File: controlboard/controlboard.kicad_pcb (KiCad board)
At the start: 4 copper layers, 65 x 56.5 mm, 167 parts, among them J1 Conn_02x04_Counter_Clockwise, J11 Pololu Voltage Regulator, J2 Conn_02x04_Row_Letter_Last, J27 GPIO, J3 Conn_02x04_Counter_Clockwise, J4 USB_C_Receptacle_USB2.0_14P, J5 Conn_02x04_Row_Letter_First, J6 Conn_02x04_Counter_Clockwise, J7 Screw_Terminal_01x02, J9 mini560 voltage regulator, Q1 PMOS AO3401A, Q2 PMOS AO3401A, SW2 SW_Push TODO FP CHECK, U2 TPS25963x, U3 AMS1117-3.3, U4 CH224K, U5 TPS25963x, U6 TPS25963x

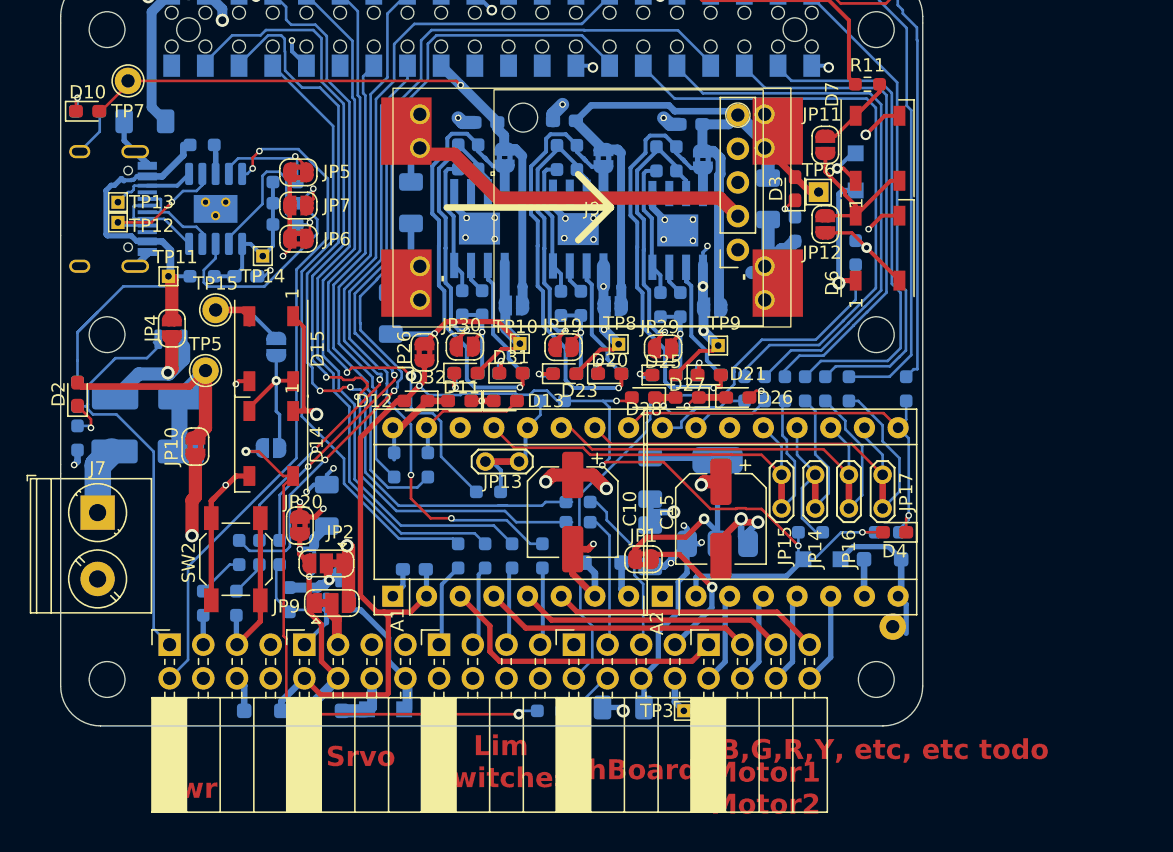
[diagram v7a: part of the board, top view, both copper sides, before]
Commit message: controlboard: fix critical mosfet errors
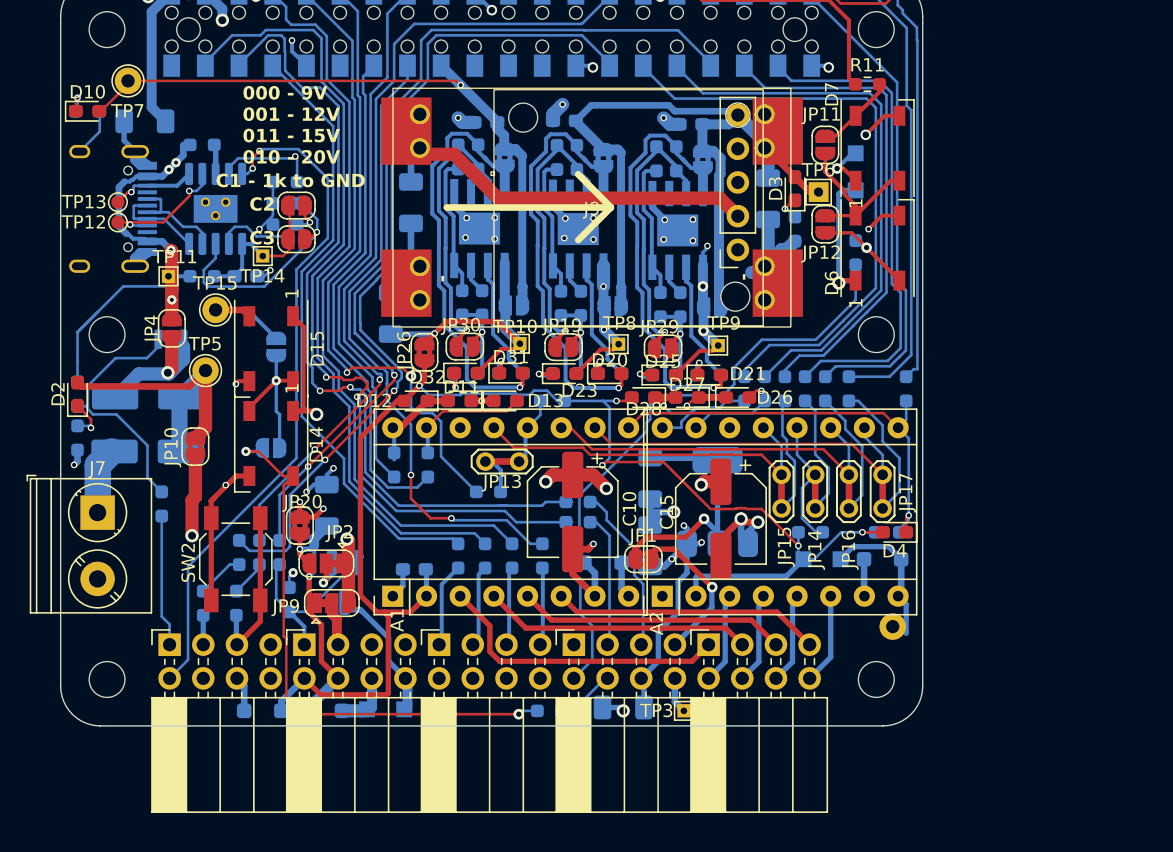
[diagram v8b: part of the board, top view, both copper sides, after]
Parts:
- removed JP5: SolderJumper_2_Bridged, Jumper:SolderJumper-2_P1.3mm_Bridged2Bar_RoundedPad1.0x1.5mm
- added R22: 10k, Resistor_SMD:R_0603_1608Metric_Pad0.98x0.95mm_HandSolder, B.Cu at (107.6, 83.3)
- JP6: value SolderJumper_2_Bridged -> CFG3; footprint Jumper:SolderJumper-2_P1.3mm_Bridged2Bar_RoundedPad1.0x1.5mm -> Jumper:SolderJumper-2_P1.3mm_Open_RoundedPad1.0x1.5mm
- JP7: value SolderJumper_2_Open -> CFG3
- Q1: value PMOS AO3401A -> NMOS AO3400A; footprint Package_TO_SOT_SMD:SOT-23 -> Package_TO_SOT_SMD:SOT-23_Handsoldering
- TP12, TP13: footprint TestPoint:TestPoint_THTPad_1.0x1.0mm_Drill0.5mm -> TestPoint:TestPoint_Pad_D1.0mm
- moved JP7 2.54 mm to (117.8, 63.3)
- moved JP6 2.50 mm to (117.8, 60.8)
- moved Q1 0.69 mm to (121.4, 89.2), turned to -90 degrees
- turned R20 to -90 degrees
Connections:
- net Net-(JP4-A) renamed /Power/VBUS
- J6 pad 7: unconnected-(J6-Pin_7-Pad7) -> GND
- JP6 pad 1: GND -> /Power/CH_VDD
- JP7 pad 1: GND -> /Power/CH_VDD
- Q1 pad 1: Net-(D1-K) -> Net-(JP9-C)
- Q1 pad 3: Net-(JP9-C) -> Net-(D1-K)
- Q2 pad 2: /Power/PWR_SW_B -> Net-(Q2-G)
- R20 pad 1: /MAG_PWM -> GND
- R20 pad 2: Net-(JP9-C) -> /MAG_PWM
- R3 pad 2: /Power/PWR_SW_B -> Net-(Q2-G)
- R4 pad 1: /Power/CH_VDD -> GND
- R5 pad 1: /Power/CH_VDD -> GND
- R6 pad 1: /Power/CH_VDD -> GND
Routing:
- net /CNC/VMOT: track 99.9 -> 158.8 mm
- net /Power/VBUS: track 44.6 -> 70.1 mm, vias 0 -> 4
- net /Power/PWR_SW_B: track 31.0 -> 9.94 mm
- net Net-(Q2-G): track 0.00 -> 19.6 mm
- net Net-(JP9-C): track 11.5 -> 3.34 mm
- net GND: track 156.0 -> 149.1 mm, vias 42 -> 43
- net Net-(JP6-B): track 14.5 -> 9.30 mm
- net /MAG_PWM: track 9.93 -> 15.0 mm
- net Net-(U4-CFG1): track 9.84 -> 7.88 mm
- net Net-(JP7-B): track 19.9 -> 17.9 mm
- net /Power/CH_VDD: track 12.0 -> 10.9 mm
- net Net-(D1-K): track 9.69 -> 10.7 mm
- net Net-(J4-CC1): track 10.7 -> 9.92 mm, vias 1 -> 2
- net Net-(J4-CC2): vias 0 -> 1
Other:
- board text added: "000 - 9V 001 - 12V 011 - 15V 010 - 20V"
- board text added: "C1 - 1k to GND"
- board text added: "C2"
- board text added: "C3"
- board text removed: "B,G,R,Y, etc, etc todo"
